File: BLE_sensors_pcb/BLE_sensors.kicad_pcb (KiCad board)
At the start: 4 copper layers, 38.2 x 25.5 mm, 50 parts, among them J1 Conn_ARM_SWD_TagConnect_TC203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, J2 Conn_01x02, J3 USB_C_Receptacle, U1 BME280, U2 LSM303AHTR, U3 TPS63031DSK, U4 ME54BS01, U5 MCP73871, U6 TLV70018_SOT23-5, U7 MCP2221AxST

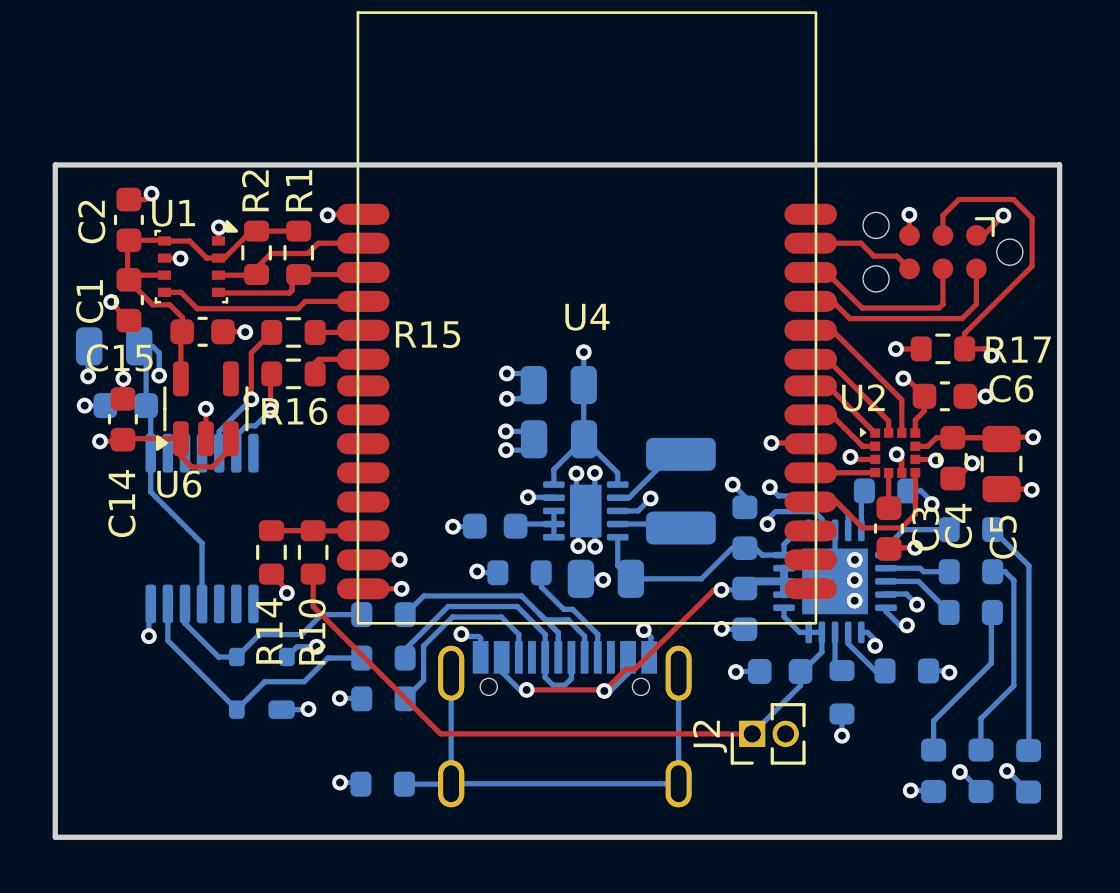
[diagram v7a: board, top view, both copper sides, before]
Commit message: Changed bme power supply and added pull up to tag connect
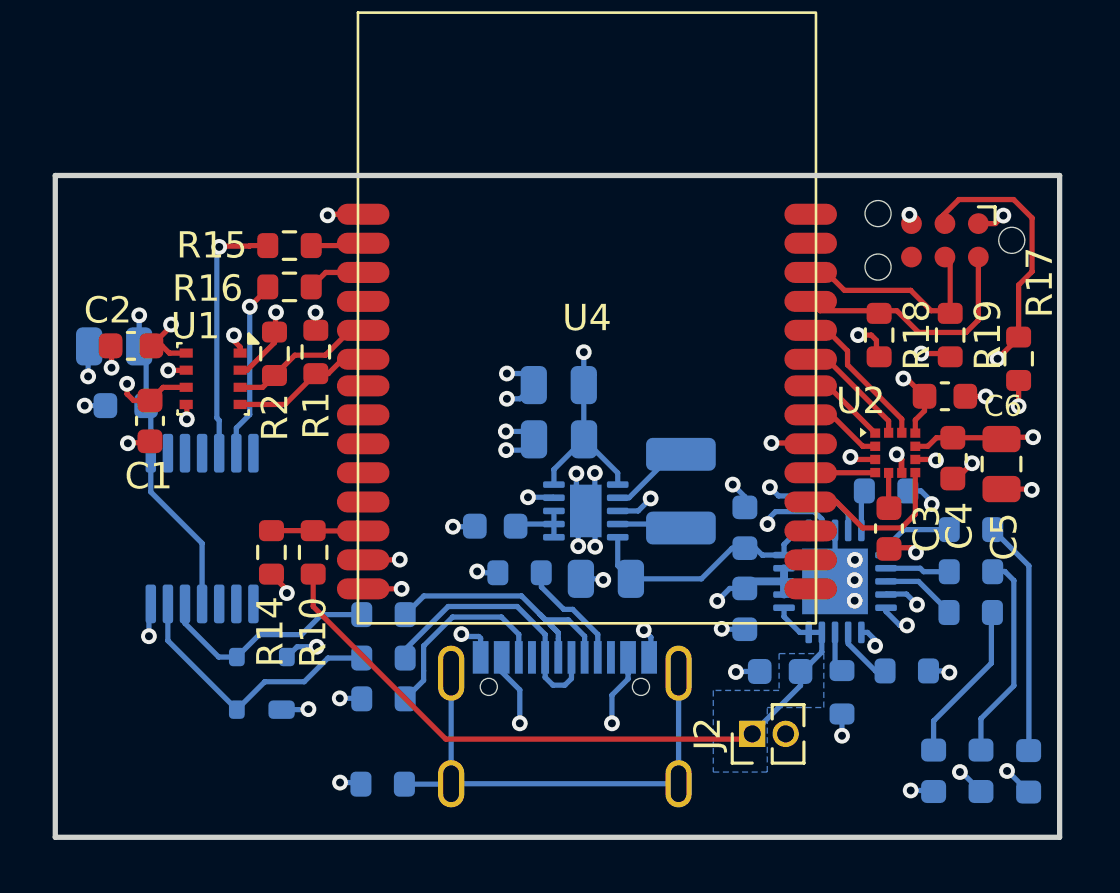
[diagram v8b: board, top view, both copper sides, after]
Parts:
- removed C14, C15: 1u, Capacitor_SMD:C_0603_1608Metric
- removed U6: TLV70018_SOT23-5, Package_TO_SOT_SMD:SOT-23-5
- added R18: 10k, Resistor_SMD:R_0603_1608Metric, F.Cu at (152.4, 73.9)
- added R19: 10k, Resistor_SMD:R_0603_1608Metric, F.Cu at (155.1, 73.9)
- moved C2 4.79 mm to (124.0, 74.3), turned to 180 degrees
- moved C1 4.65 mm to (124.7, 77.2)
- moved U1 4.34 mm to (127.1, 75.6)
- moved R2 3.89 mm to (129.4, 74.6)
- moved R1 3.82 mm to (131.0, 74.5)
- moved R16 3.31 mm to (130.0, 72.1)
- moved R15 3.30 mm to (130.0, 70.5)
- moved R17 2.90 mm to (157.7, 74.8), turned to -90 degrees
- moved J1 0.46 mm to (154.9, 70.3)
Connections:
- C1 pad 1: +1V8 -> +3V3
- C2 pad 1: +1V8 -> +3V3
- J1 pad 6: /SWO -> unconnected-(J1-SWO-Pad6)
- R1 pad 2: +1V8 -> +3V3
- R2 pad 2: +1V8 -> +3V3
- U1 pad 2: +1V8 -> +3V3
- U1 pad 5: /SDO -> GND
- U1 pad 6: +1V8 -> +3V3
- U1 pad 8: +1V8 -> +3V3
- U4 pad 2: /SDA -> /TX
- U4 pad 27: /SWO -> unconnected-(U4-P0.02-Pad27)
- U4 pad 3: /SCL -> /RX
- U4 pad 4: /SDO -> unconnected-(U4-P1.11/AIN4-Pad4)
- U4 pad 5: /TX -> /SDA
- U4 pad 6: /RX -> /SCL
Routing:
- net +1V8: track 15.1 -> 0.00 mm
- net /SDO: track 7.92 -> 0.00 mm
- net +5V: track 27.5 -> 21.1 mm
- net Net-(U7-URx): track 5.41 -> 9.78 mm
- net /SWO: track 4.16 -> 0.00 mm
- net Net-(U7-UTx): track 3.77 -> 6.81 mm
- net /SWDIO: track 8.14 -> 10.4 mm
- net +3V3: track 40.8 -> 43.0 mm, vias 9 -> 13
- net /nRESET: track 23.1 -> 21.6 mm
- net GND: track 51.5 -> 50.2 mm, vias 50 -> 49
- net /SWCLK: track 6.99 -> 8.07 mm
- net /SCL: track 6.04 -> 5.39 mm
- added copper zone on B.Cu, net +V_bat
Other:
- board size 38.2 x 25.5 mm -> 38.2 x 25.1 mm
